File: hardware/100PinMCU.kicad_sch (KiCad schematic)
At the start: 28 parts, among them J5 SWD_Header_02x02, U2 STM32G491VET6_1, Y1 Crystal

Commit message: why is everything weird
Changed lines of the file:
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@@
 	)
 	(hierarchical_label "BOOT"
-		(shape bidirectional)
+		(shape input)
 		(at 128.905 106.045 0)
 		(effects

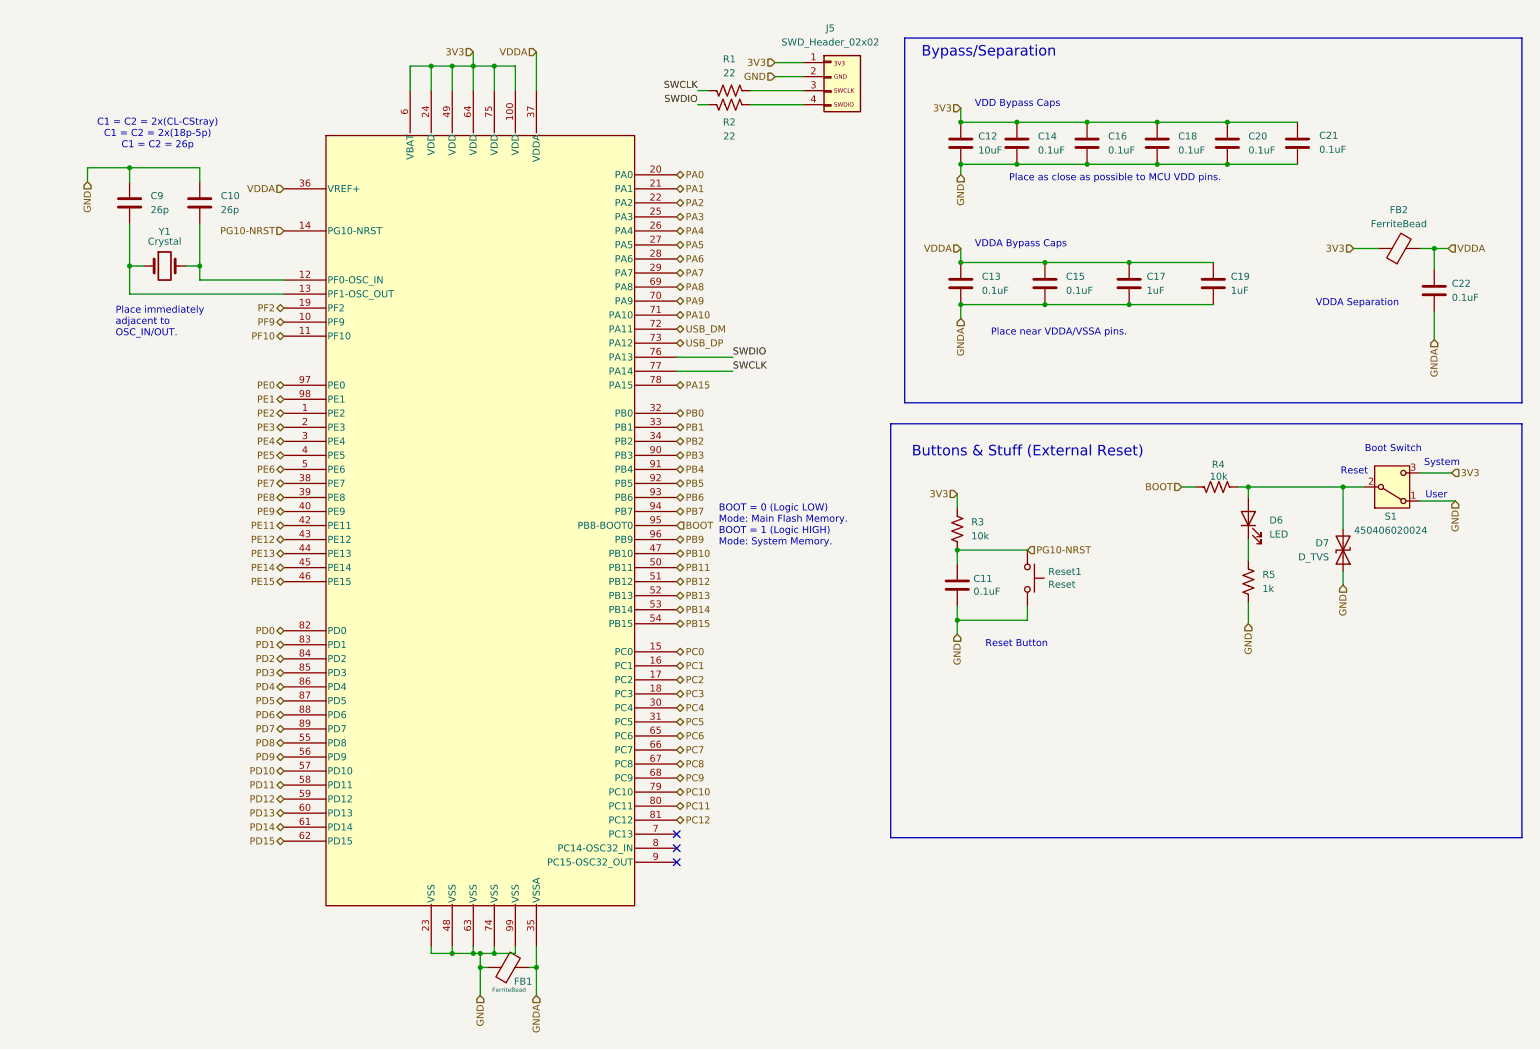
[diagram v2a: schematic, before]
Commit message: finished schematic except for 12v buck boost
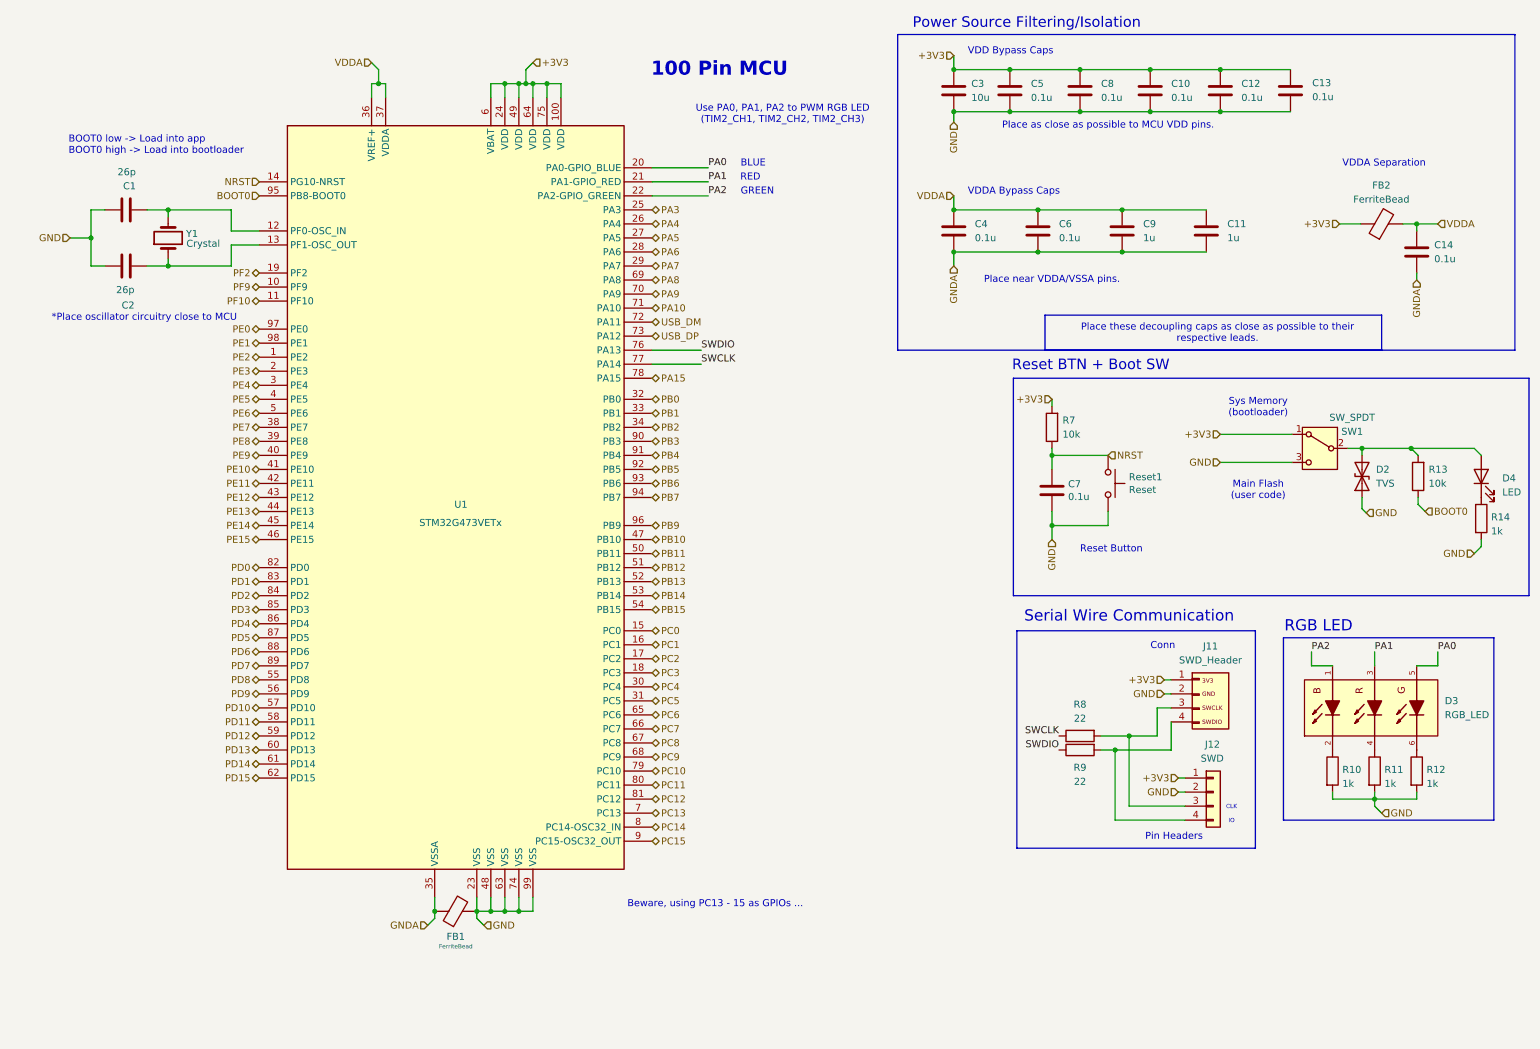
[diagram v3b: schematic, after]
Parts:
- removed C10, C9: 26p, Capacitor_SMD:C_0603_1608Metric_Pad1.08x0.95mm_HandSolder, symbol Device:C
- removed C11, C13: 0.1uF, Capacitor_SMD:C_0603_1608Metric_Pad1.08x0.95mm_HandSolder, symbol Device:C
- removed C12: 10uF, Capacitor_SMD:C_0805_2012Metric, symbol Device:C
- removed D6: LED, LED_SMD:LED_0201_0603Metric, symbol Device:LED
- removed D7: D_TVS, Diode_SMD:D_SOD-323, symbol Device:D_TVS
- removed R1, R2: 22, Resistor_SMD:R_0603_1608Metric_Pad0.98x0.95mm_HandSolder, symbol Device:R_US
- removed R4: 10k, Resistor_SMD:R_0603_1608Metric_Pad0.98x0.95mm_HandSolder, symbol Device:R_US
- removed R5: 1k, Resistor_SMD:R_0603_1608Metric_Pad0.98x0.95mm_HandSolder, symbol Device:R_US
- removed S1: 450406020024, UTSVT_Special:BootSW, symbol Switch:SW_SPDT
- removed U2: STM32G491VET6_1, UTSVT_ICs:LQFP_491VET6_STM, symbol utsvt_ics:STM32G491VET6_1
- added C1, C2: 26p, Capacitor_SMD:C_0603_1608Metric_Pad1.08x0.95mm_HandSolder, symbol Device:C
- added C3: 10u, Capacitor_SMD:C_0805_2012Metric_Pad1.18x1.45mm_HandSolder, symbol Device:C
- added C4, C7: 0.1u, Capacitor_SMD:C_0603_1608Metric_Pad1.08x0.95mm_HandSolder, symbol Device:C
- added D2: TVS, Diode_SMD:D_SOD-323, symbol lhrs_misc:Boot_TVS
- added D3: RGB_LED, LHRS_Special:RGB_LED, symbol lhrs_special:RGB_LED
- added D4: LED, LED_SMD:LED_0603_1608Metric_Pad1.05x0.95mm_HandSolder, symbol lhrs_misc:Blue_LED
- added J12: SWD, Connector_PinHeader_2.54mm:PinHeader_1x04_P2.54mm_Vertical, symbol Connector_Generic:Conn_01x04
- added R10, R11, R12, R14: 1k, Resistor_SMD:R_0603_1608Metric_Pad0.98x0.95mm_HandSolder, symbol Device:R
- added R13: 10k, Resistor_SMD:R_0603_1608Metric_Pad0.98x0.95mm_HandSolder, symbol Device:R
- added R8, R9: 22, Resistor_SMD:R_0603_1608Metric_Pad0.98x0.95mm_HandSolder, symbol Device:R
- added SW1: SW_SPDT, LHRS_Special:BootSW, symbol Switch:SW_SPDT
- added U1: STM32G473VETx, LHRS_Special:100PinMCU, symbol lhrs_special:STM32G473VET6
- C10: renamed from C18; value 0.1uF -> 0.1u
- C11: renamed from C19; value 1uF -> 1u
- C12: renamed from C20; value 0.1uF -> 0.1u
- C13: renamed from C21; value 0.1uF -> 0.1u
- C14: renamed from C22; value 0.1uF -> 0.1u
- C5: renamed from C14; value 0.1uF -> 0.1u
- C6: renamed from C15; value 0.1uF -> 0.1u
- C8: renamed from C16; value 0.1uF -> 0.1u
- C9: renamed from C17; value 1uF -> 1u
- FB1, FB2: footprint Capacitor_SMD:C_0603_1608Metric_Pad1.08x0.95mm_HandSolder -> Inductor_SMD:L_0805_2012Metric_Pad1.05x1.20mm_HandSolder
- J11: renamed from J5; value SWD_Header_02x02 -> SWD_Header; footprint UTSVT_Connectors:SWD_Conn -> LHRS_Connectors:SWD_Conn
- R7: renamed from R3; symbol Device:R_US -> Device:R
- Reset1: footprint UTSVT_Special:TL3365AF180QG -> LHRS_Special:TL3365AF180QG
- Y1: footprint UTSVT_Passives:Crystal_SMD_Abracon_ABM3-2Pin_5.0x3.2mm -> LHRS_Passives:Crystal_SMD_Abracon_ABM3-2Pin_5.0x3.2mm
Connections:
- net GND: now also FB1.2, C1.1, C2.1, C3.2, C7.2, D2.1 (A1), J12.2 (Pin_2), R10.2, R11.2, R12.2, R14.2, SW1.3 (C), U1.23 (VSS), U1.48 (VSS), U1.63 (VSS), U1.74 (VSS), U1.99 (VSS); no longer FB1.1
- net GNDA: now also FB1.1, C4.2, U1.35 (VSSA); no longer FB1.2
- net PA0: now also D3.5, U1.20 (PA0-GPIO_BLUE)
- net PA1: now also D3.3, U1.21 (PA1-GPIO_RED)
- net PA10: now also U1.71 (PA10)
- net PA15: now also U1.78 (PA15)
- net PA2: now also D3.1, U1.22 (PA2-GPIO_GREEN)
- net PA3: now also U1.25 (PA3)
- net PA4: now also U1.26 (PA4)
- net PA5: now also U1.27 (PA5)
- net PA6: now also U1.28 (PA6)
- net PA7: now also U1.29 (PA7)
- net PA8: now also U1.69 (PA8)
- net PA9: now also U1.70 (PA9)
- net PB0: now also U1.32 (PB0)
- net PB1: now also U1.33 (PB1)
- net PB10: now also U1.47 (PB10)
- net PB11: now also U1.50 (PB11)
- net PB12: now also U1.51 (PB12)
- net PB13: now also U1.52 (PB13)
- net PB14: now also U1.53 (PB14)
- net PB15: now also U1.54 (PB15)
- net PB2: now also U1.34 (PB2)
- net PB3: now also U1.90 (PB3)
- net PB4: now also U1.91 (PB4)
- net PB5: now also U1.92 (PB5)
- net PB6: now also U1.93 (PB6)
- net PB7: now also U1.94 (PB7)
- net PB9: now also U1.96 (PB9)
- net PC0: now also U1.15 (PC0)
- net PC1: now also U1.16 (PC1)
- net PC10: now also U1.79 (PC10)
- net PC11: now also U1.80 (PC11)
- net PC12: now also U1.81 (PC12)
- net PC2: now also U1.17 (PC2)
- net PC3: now also U1.18 (PC3)
- net PC4: now also U1.30 (PC4)
- net PC5: now also U1.31 (PC5)
- net PC6: now also U1.65 (PC6)
- net PC7: now also U1.66 (PC7)
- net PC8: now also U1.67 (PC8)
- net PC9: now also U1.68 (PC9)
- net PD0: now also U1.82 (PD0)
- net PD1: now also U1.83 (PD1)
- net PD10: now also U1.57 (PD10)
- net PD11: now also U1.58 (PD11)
- net PD12: now also U1.59 (PD12)
- net PD13: now also U1.60 (PD13)
- net PD14: now also U1.61 (PD14)
- net PD15: now also U1.62 (PD15)
- net PD2: now also U1.84 (PD2)
- net PD3: now also U1.85 (PD3)
- net PD4: now also U1.86 (PD4)
- net PD5: now also U1.87 (PD5)
- net PD6: now also U1.88 (PD6)
- net PD7: now also U1.89 (PD7)
- net PD8: now also U1.55 (PD8)
- net PD9: now also U1.56 (PD9)
- net PE0: now also U1.97 (PE0)
- net PE1: now also U1.98 (PE1)
- net PE11: now also U1.42 (PE11)
- net PE12: now also U1.43 (PE12)
- net PE13: now also U1.44 (PE13)
- net PE14: now also U1.45 (PE14)
- net PE15: now also U1.46 (PE15)
- net PE2: now also U1.1 (PE2)
- net PE3: now also U1.2 (PE3)
- net PE4: now also U1.3 (PE4)
- net PE5: now also U1.4 (PE5)
- net PE6: now also U1.5 (PE6)
- net PE7: now also U1.38 (PE7)
- net PE8: now also U1.39 (PE8)
- net PE9: now also U1.40 (PE9)
- net PF10: now also U1.11 (PF10)
- net PF2: now also U1.19 (PF2)
- net PF9: now also U1.10 (PF9)
- net SWCLK: now also R8.1, U1.77 (PA14)
- net SWDIO: now also R9.1, U1.76 (PA13)
- net USB_DM: now also U1.72 (PA11)
- net USB_DP: now also U1.73 (PA12)
- net VDDA: now also C4.1, U1.36 (VREF+), U1.37 (VDDA)
- net at Y1.1: now also C2.2, U1.13 (PF1-OSC_OUT)
- net at Y1.2: now also C1.2, U1.12 (PF0-OSC_IN)
- net at J11.3 (Pin_3): now also J12.3 (Pin_3), R8.2
- net at J11.4 (Pin_4): now also J12.4 (Pin_4), R9.2
- net 3V3 renamed +3V3
- net +3V3: now also C3.1, J12.1 (Pin_1), SW1.1 (A), U1.100 (VDD), U1.24 (VDD), U1.49 (VDD), U1.6 (VBAT), U1.64 (VDD), U1.75 (VDD)
- net PG10-NRST renamed NRST
- net NRST: now also C7.1, U1.14 (PG10-NRST)
- new net: D2.2 (A2), D4.2 (A), R13.2, SW1.2 (B)
- new net: D4.1 (K), R14.1
- new net: D3.2, R10.1
- new net: D3.4, R11.1
- new net: D3.6, R12.1
- new net BOOT0: R13.1, U1.95 (PB8-BOOT0)
- new net PC13: U1.7 (PC13)
- new net PC14: U1.8 (PC14-OSC32_IN)
- new net PC15: U1.9 (PC15-OSC32_OUT)
- new net PE10: U1.41 (PE10)
- no-connect marks 3 -> 0
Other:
- note added: "*Place oscillator circuitry close to MCU"
- note added: "100 Pin MCU"
- note added: "BLUE"
- note added: "BOOT0 low -> Load into app BOOT0 high -> Load into bootloader"
- note added: "Beware, using PC13 - 15 as GPIOs ..."
- note added: "CLK"
- note added: "Conn"
- note added: "GREEN"
- note added: "IO"
- note added: "Main Flash (user code)"
- note added: "Pin Headers"
- note added: "Place these decoupling caps as close as possible to their respective leads."
- note added: "Power Source Filtering/Isolation"
- note added: "RED"
- note added: "RGB LED"
- note added: "Reset BTN + Boot SW"
- note added: "Serial Wire Communication"
- note added: "Sys Memory (bootloader)"
- note added: "Use PA0, PA1, PA2 to PWM RGB LED (TIM2_CH1, TIM2_CH2, TIM2_CH3)"
- note removed: "BOOT = 0 (Logic LOW) Mode: Main Flash Memory. BOOT = 1 (Logic HIGH) Mode: System Memory."
- note removed: "Boot Switch"
- note removed: "Buttons & Stuff (External Reset)"
- note removed: "Bypass/Separation"
- note removed: "C1 = C2 = 2x(CL-CStray) C1 = C2 = 2x(18p-5p) C1 = C2 = 26p"
- note removed: "Place immediately adjacent to OSC_IN/OUT."
- note removed: "Reset"
- note removed: "System"
- note removed: "User"
- moved on the sheet: C10, C11, C12, C13, C14, C5, C6, C8, C9, FB2, J11, Reset1

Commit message: added 12V buck boost
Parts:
- renumbered C9 to C10, C10 to C11, C11 to C12, C12 to C13, C13 to C14, C14 to C15, C1 to C2, C2 to C3, C3 to C4, C4 to C5, C5 to C6, C6 to C7, C7 to C8, C8 to C9, D2 to D4, D3 to D5, D4 to D6, R7 to R11, R8 to R12, R9 to R13, R10 to R14, R11 to R15, R12 to R16, R13 to R17, R14 to R18
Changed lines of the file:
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@@
 		(dnp no)
 		(fields_autoplaced yes)
-		(property "Reference" "C9"
+		(property "Reference" "C10"
 			(at 213.36 51.4349 0)
 			(show_name no)
@@
 			(project "PS-BPSLeader"
 				(path "/d4a4ed4f-0983-4aef-b212-0e3284ab3963/5da56964-fa04-4fec-bdfe-c6acfeda5c9a/972ee48b-c33c-4022-a95a-ebc71c386daa"
-					(reference "C9")
+					(reference "C10")
 					(unit 1)
 				)
@@
 		(dnp no)
 		(fields_autoplaced yes)
-		(property "Reference" "R7"
+		(property "Reference" "R11"
 			(at 198.755 86.9949 0)
 			(show_name no)
@@
 			(project "PS-BPSLeader"
 				(path "/d4a4ed4f-0983-4aef-b212-0e3284ab3963/5da56964-fa04-4fec-bdfe-c6acfeda5c9a/972ee48b-c33c-4022-a95a-ebc71c386daa"
-					(reference "R7")
+					(reference "R11")
 					(unit 1)
 				)
@@
 		(in_pos_files yes)
 		(dnp no)
-		(property "Reference" "C7"
+		(property "Reference" "C8"
 			(at 199.771 98.5266 0)
 			(show_name no)
@@
 			(project "PS-BPSLeader"
 				(path "/d4a4ed4f-0983-4aef-b212-0e3284ab3963/5da56964-fa04-4fec-bdfe-c6acfeda5c9a/972ee48b-c33c-4022-a95a-ebc71c386daa"
-					(reference "C7")
+					(reference "C8")
 					(unit 1)
 				)
@@
 		(dnp no)
 		(fields_autoplaced yes)
-		(property "Reference" "D2"
+		(property "Reference" "D4"
 			(at 255.524 95.8849 90)
 			(show_name no)
@@
 			(project "PS-BPSLeader"
 				(path "/d4a4ed4f-0983-4aef-b212-0e3284ab3963/5da56964-fa04-4fec-bdfe-c6acfeda5c9a/972ee48b-c33c-4022-a95a-ebc71c386daa"
-					(reference "D2")
+					(reference "D4")
 					(unit 1)
 				)
@@
 		(dnp no)
 		(fields_autoplaced yes)
-		(property "Reference" "D4"
+		(property "Reference" "D6"
 			(at 278.384 97.4724 90)
 			(show_name no)
@@
 			(project "PS-BPSLeader"
 				(path "/d4a4ed4f-0983-4aef-b212-0e3284ab3963/5da56964-fa04-4fec-bdfe-c6acfeda5c9a/972ee48b-c33c-4022-a95a-ebc71c386daa"
-					(reference "D4")
+					(reference "D6")
 					(unit 1)
 				)
@@
 		(in_pos_files yes)
 		(dnp no)
-		(property "Reference" "C1"
+		(property "Reference" "C2"
 			(at 30.988 44.577 90)
 			(show_name no)
@@
 			(project "PS-BPSLeader"
 				(path "/d4a4ed4f-0983-4aef-b212-0e3284ab3963/5da56964-fa04-4fec-bdfe-c6acfeda5c9a/972ee48b-c33c-4022-a95a-ebc71c386daa"
-					(reference "C1")
+					(reference "C2")
 					(unit 1)
 				)
@@
 		(in_pos_files yes)
 		(dnp no)
-		(property "Reference" "R14"
+		(property "Reference" "R18"
 			(at 276.352 104.521 0)
 			(show_name no)
@@
 			(project "PS-BPSLeader"
 				(path "/d4a4ed4f-0983-4aef-b212-0e3284ab3963/5da56964-fa04-4fec-bdfe-c6acfeda5c9a/972ee48b-c33c-4022-a95a-ebc71c386daa"
-					(reference "R14")
+					(reference "R18")
 					(unit 1)
 				)
@@
 		(in_pos_files yes)
 		(dnp no)
-		(property "Reference" "R13"
+		(property "Reference" "R17"
 			(at 265.049 95.8849 0)
 			(show_name no)
@@
 			(project "PS-BPSLeader"
 				(path "/d4a4ed4f-0983-4aef-b212-0e3284ab3963/5da56964-fa04-4fec-bdfe-c6acfeda5c9a/972ee48b-c33c-4022-a95a-ebc71c386daa"
-					(reference "R13")
+					(reference "R17")
 					(unit 1)
 				)
@@
 		(dnp no)
 		(fields_autoplaced yes)
-		(property "Reference" "C6"
+		(property "Reference" "C7"
 			(at 198.12 51.4349 0)
 			(show_name no)
@@
 			(project "PS-BPSLeader"
 				(path "/d4a4ed4f-0983-4aef-b212-0e3284ab3963/5da56964-fa04-4fec-bdfe-c6acfeda5c9a/972ee48b-c33c-4022-a95a-ebc71c386daa"
-					(reference "C6")
+					(reference "C7")
 					(unit 1)
 				)
@@
 		(dnp no)
 		(fields_autoplaced yes)
-		(property "Reference" "C5"
+		(property "Reference" "C6"
 			(at 193.04 26.0349 0)
 			(show_name no)
@@
 			(project "PS-BPSLeader"
 				(path "/d4a4ed4f-0983-4aef-b212-0e3284ab3963/5da56964-fa04-4fec-bdfe-c6acfeda5c9a/972ee48b-c33c-4022-a95a-ebc71c386daa"
-					(reference "C5")
+					(reference "C6")
 					(unit 1)
 				)
@@
 		(in_pos_files yes)
 		(dnp no)
-		(property "Reference" "C2"
+		(property "Reference" "C3"
 			(at 30.734 66.167 90)
 			(show_name no)
@@
 			(project "PS-BPSLeader"
 				(path "/d4a4ed4f-0983-4aef-b212-0e3284ab3963/5da56964-fa04-4fec-bdfe-c6acfeda5c9a/972ee48b-c33c-4022-a95a-ebc71c386daa"
-					(reference "C2")
+					(reference "C3")
 					(unit 1)
 				)
@@
 		(dnp no)
 		(fields_autoplaced yes)
-		(property "Reference" "C10"
+		(property "Reference" "C11"
 			(at 218.44 26.0349 0)
 			(show_name no)
@@
 			(project "PS-BPSLeader"
 				(path "/d4a4ed4f-0983-4aef-b212-0e3284ab3963/5da56964-fa04-4fec-bdfe-c6acfeda5c9a/972ee48b-c33c-4022-a95a-ebc71c386daa"
-					(reference "C10")
+					(reference "C11")
 					(unit 1)
 				)
@@
 		(dnp no)
 		(fields_autoplaced yes)
-		(property "Reference" "C12"
+		(property "Reference" "C13"
 			(at 231.14 26.0349 0)
 			(show_name no)
@@
 			(project "PS-BPSLeader"
 				(path "/d4a4ed4f-0983-4aef-b212-0e3284ab3963/5da56964-fa04-4fec-bdfe-c6acfeda5c9a/972ee48b-c33c-4022-a95a-ebc71c386daa"
-					(reference "C12")
+					(reference "C13")
 					(unit 1)
 				)
@@
 		(in_pos_files yes)
 		(dnp no)
-		(property "Reference" "R9"
+		(property "Reference" "R13"
 			(at 201.93 149.86 90)
 			(show_name no)
@@
 			(project "PS-BPSLeader"
 				(path "/d4a4ed4f-0983-4aef-b212-0e3284ab3963/5da56964-fa04-4fec-bdfe-c6acfeda5c9a/972ee48b-c33c-4022-a95a-ebc71c386daa"
-					(reference "R9")
+					(reference "R13")
 					(unit 1)
 				)
@@
 		(dnp no)
 		(fields_autoplaced yes)
-		(property "Reference" "C3"
+		(property "Reference" "C4"
 			(at 182.245 26.0349 0)
 			(show_name no)
@@
 			(project "PS-BPSLeader"
 				(path "/d4a4ed4f-0983-4aef-b212-0e3284ab3963/5da56964-fa04-4fec-bdfe-c6acfeda5c9a/972ee48b-c33c-4022-a95a-ebc71c386daa"
-					(reference "C3")
+					(reference "C4")
 					(unit 1)
 				)
@@
 		(dnp no)
 		(fields_autoplaced yes)
-		(property "Reference" "C4"
+		(property "Reference" "C5"
 			(at 182.88 51.4349 0)
 			(show_name no)
@@
 			(project "PS-BPSLeader"
 				(path "/d4a4ed4f-0983-4aef-b212-0e3284ab3963/5da56964-fa04-4fec-bdfe-c6acfeda5c9a/972ee48b-c33c-4022-a95a-ebc71c386daa"
-					(reference "C4")
+					(reference "C5")
 					(unit 1)
 				)
@@
 		(dnp no)
 		(fields_autoplaced yes)
-		(property "Reference" "D3"
+		(property "Reference" "D5"
 			(at 267.97 137.7949 90)
 			(show_name no)
@@
 			(project "PS-BPSLeader"
 				(path "/d4a4ed4f-0983-4aef-b212-0e3284ab3963/5da56964-fa04-4fec-bdfe-c6acfeda5c9a/972ee48b-c33c-4022-a95a-ebc71c386daa"
-					(reference "D3")
+					(reference "D5")
 					(unit 1)
 				)
@@
 		(dnp no)
 		(fields_autoplaced yes)
-		(property "Reference" "C11"
+		(property "Reference" "C12"
 			(at 228.6 51.4349 0)
 			(show_name no)
@@
 			(project "PS-BPSLeader"
 				(path "/d4a4ed4f-0983-4aef-b212-0e3284ab3963/5da56964-fa04-4fec-bdfe-c6acfeda5c9a/972ee48b-c33c-4022-a95a-ebc71c386daa"
-					(reference "C11")
+					(reference "C12")
 					(unit 1)
 				)
@@
 		(in_pos_files yes)
 		(dnp no)
-		(property "Reference" "R11"
+		(property "Reference" "R15"
 			(at 257.048 150.241 0)
 			(show_name no)
@@
 			(project "PS-BPSLeader"
 				(path "/d4a4ed4f-0983-4aef-b212-0e3284ab3963/5da56964-fa04-4fec-bdfe-c6acfeda5c9a/972ee48b-c33c-4022-a95a-ebc71c386daa"
-					(reference "R11")
+					(reference "R15")
 					(unit 1)
 				)
@@
 		(dnp no)
 		(fields_autoplaced yes)
-		(property "Reference" "C14"
+		(property "Reference" "C15"
 			(at 266.065 55.2449 0)
 			(show_name no)
@@
 			(project "PS-BPSLeader"
 				(path "/d4a4ed4f-0983-4aef-b212-0e3284ab3963/5da56964-fa04-4fec-bdfe-c6acfeda5c9a/972ee48b-c33c-4022-a95a-ebc71c386daa"
-					(reference "C14")
+					(reference "C15")
 					(unit 1)
 				)
@@
 		(dnp no)
 		(fields_autoplaced yes)
-		(property "Reference" "C8"
+		(property "Reference" "C9"
 			(at 205.74 26.0349 0)
 			(show_name no)
@@
 			(project "PS-BPSLeader"
 				(path "/d4a4ed4f-0983-4aef-b212-0e3284ab3963/5da56964-fa04-4fec-bdfe-c6acfeda5c9a/972ee48b-c33c-4022-a95a-ebc71c386daa"
-					(reference "C8")
+					(reference "C9")
 					(unit 1)
 				)
@@
 		(in_pos_files yes)
 		(dnp no)
-		(property "Reference" "R10"
+		(property "Reference" "R14"
 			(at 249.428 150.241 0)
 			(show_name no)
@@
 			(project "PS-BPSLeader"
 				(path "/d4a4ed4f-0983-4aef-b212-0e3284ab3963/5da56964-fa04-4fec-bdfe-c6acfeda5c9a/972ee48b-c33c-4022-a95a-ebc71c386daa"
-					(reference "R10")
+					(reference "R14")
 					(unit 1)
 				)
@@
 		(in_pos_files yes)
 		(dnp no)
-		(property "Reference" "R12"
+		(property "Reference" "R16"
 			(at 264.668 150.241 0)
 			(show_name no)
@@
 			(project "PS-BPSLeader"
 				(path "/d4a4ed4f-0983-4aef-b212-0e3284ab3963/5da56964-fa04-4fec-bdfe-c6acfeda5c9a/972ee48b-c33c-4022-a95a-ebc71c386daa"
-					(reference "R12")
+					(reference "R16")
 					(unit 1)
 				)
@@
 		(dnp no)
 		(fields_autoplaced yes)
-		(property "Reference" "R8"
+		(property "Reference" "R12"
 			(at 201.93 138.43 90)
 			(show_name no)
@@
 			(project "PS-BPSLeader"
 				(path "/d4a4ed4f-0983-4aef-b212-0e3284ab3963/5da56964-fa04-4fec-bdfe-c6acfeda5c9a/972ee48b-c33c-4022-a95a-ebc71c386daa"
-					(reference "R8")
+					(reference "R12")
 					(unit 1)
 				)
@@
 		(in_pos_files yes)
 		(dnp no)
-		(property "Reference" "C13"
+		(property "Reference" "C14"
 			(at 243.967 25.908 0)
 			(show_name no)
@@
 			(project "PS-BPSLeader"
 				(path "/d4a4ed4f-0983-4aef-b212-0e3284ab3963/5da56964-fa04-4fec-bdfe-c6acfeda5c9a/972ee48b-c33c-4022-a95a-ebc71c386daa"
-					(reference "C13")
+					(reference "C14")
 					(unit 1)
 				)

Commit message: papercut -linkin park
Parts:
- FB1, FB2: footprint Inductor_SMD:L_0805_2012Metric_Pad1.05x1.20mm_HandSolder -> Inductor_SMD:L_0603_1608Metric_Pad1.05x0.95mm_HandSolder
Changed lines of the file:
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@@
 			)
 		)
-		(property "Footprint" "Inductor_SMD:L_0805_2012Metric_Pad1.05x1.20mm_HandSolder"
+		(property "Footprint" "Inductor_SMD:L_0603_1608Metric_Pad1.05x0.95mm_HandSolder"
 			(at 256.54 53.213 90)
 			(hide yes)
@@
 			)
 		)
-		(property "Footprint" "Inductor_SMD:L_0805_2012Metric_Pad1.05x1.20mm_HandSolder"
+		(property "Footprint" "Inductor_SMD:L_0603_1608Metric_Pad1.05x0.95mm_HandSolder"
 			(at 88.9 177.673 90)
 			(hide yes)
